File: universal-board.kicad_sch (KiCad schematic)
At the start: 15 parts, among them J1 USB_C_Receptacle, J2 CONN_I2C_GROVE, J3 CONN_WS2812, SW1 SW_RESET, U1 USBLC6-2SC6, U2 USBLC6-2SC6, U3 ESP32-S3-WROOM-1, U4 AMS1117-3.3

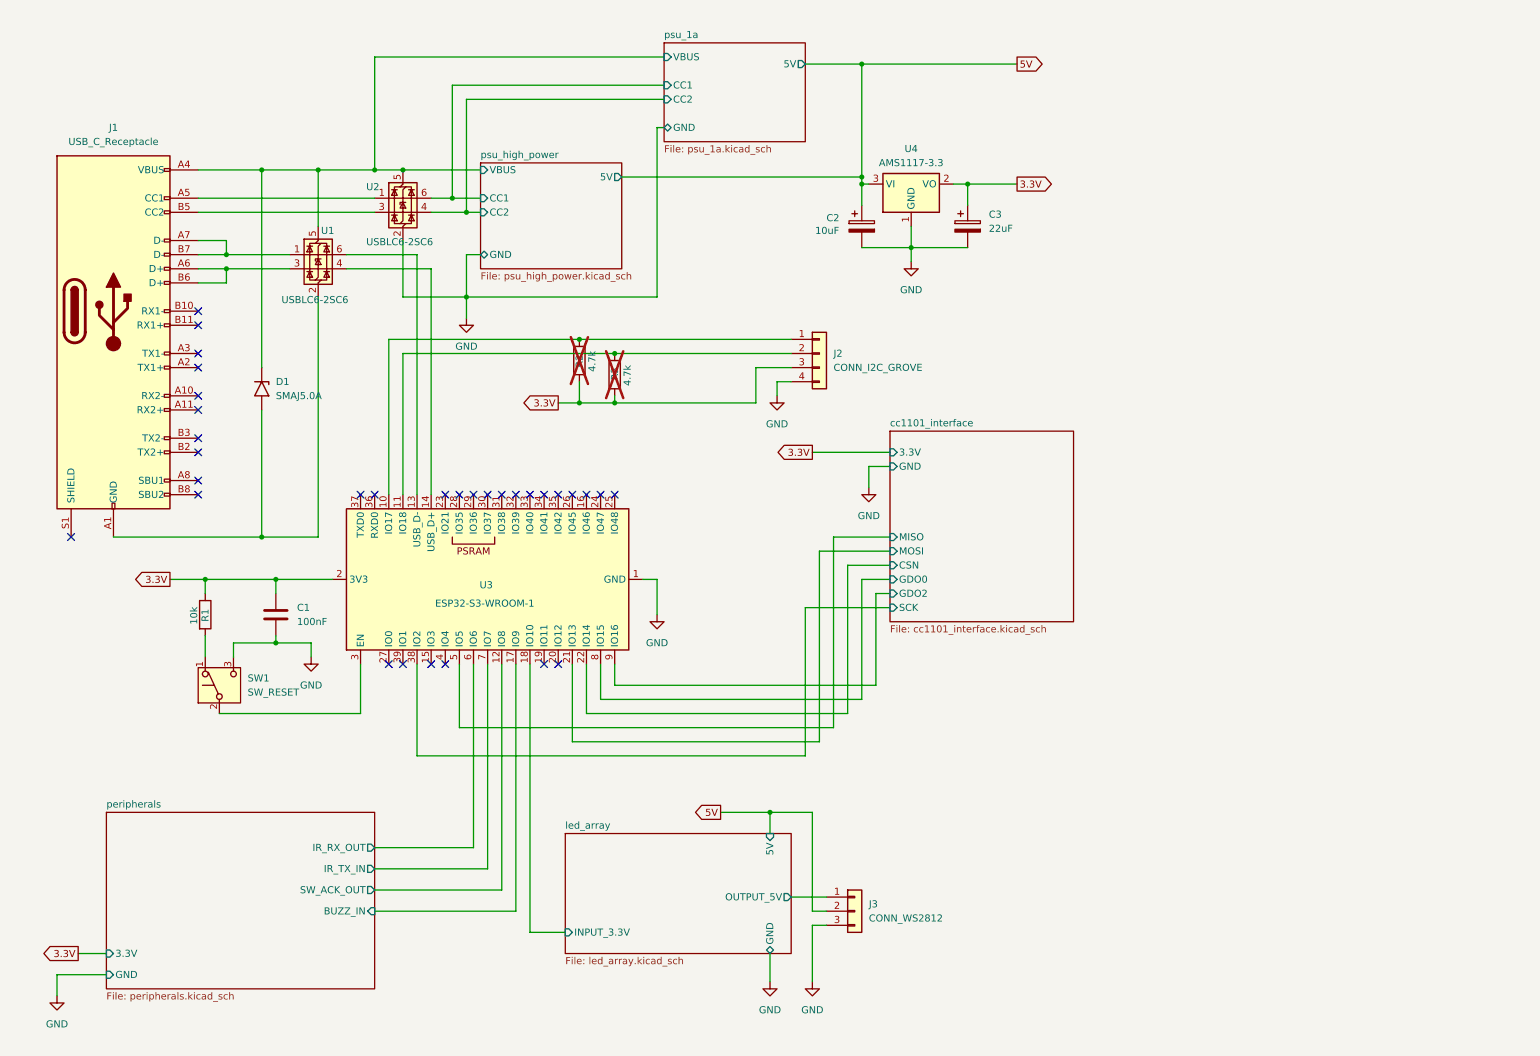
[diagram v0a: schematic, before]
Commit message: ERC fixes.
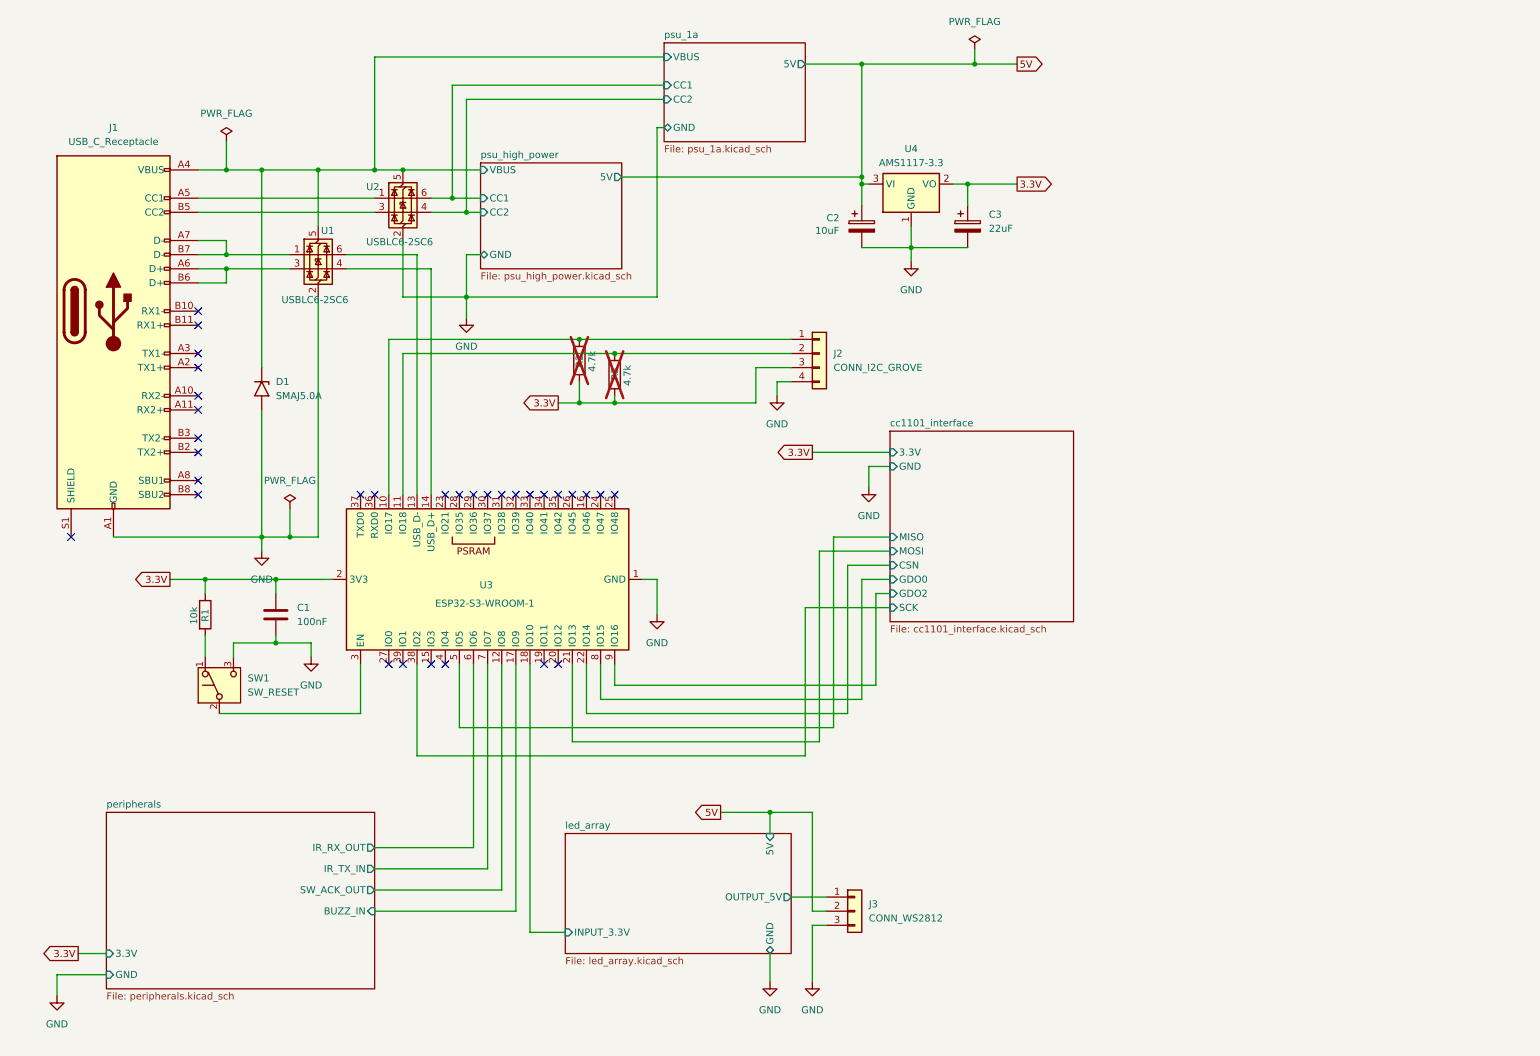
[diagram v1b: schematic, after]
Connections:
- net GND: now also D1.2 (A2), J1.A1 (GND), J1.A12 (GND), J1.B1 (GND), J1.B12 (GND), U1.2 (GND)

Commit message: - added bidirectional TVS between VBUS & GND - USB-C shield and GND are now connected - added comments re pin order - removed pull-up resistor on SW_ACK_INPUT because it's configured as INPUT_PULLUP
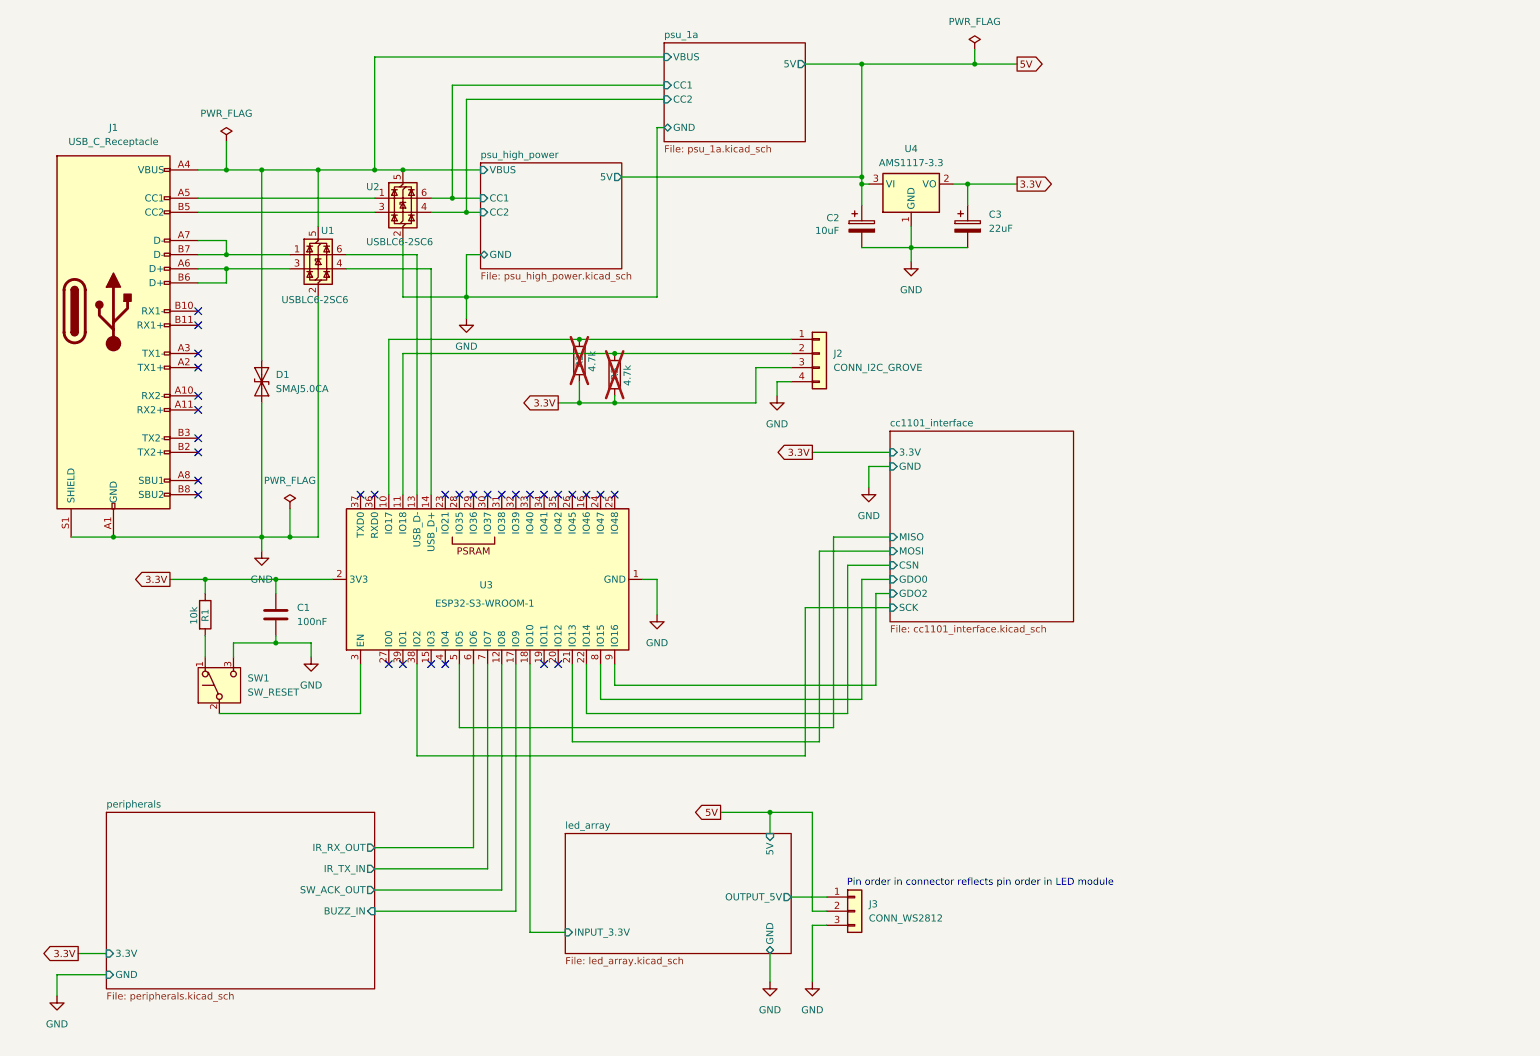
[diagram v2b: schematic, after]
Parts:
- removed D1: SMAJ5.0A, Diode_SMD:D_SMA, symbol Diode:SMAJ5.0A
- added D1: SMAJ5.0CA, Diode_SMD:D_SMA, symbol Diode:SMAJ5.0CA
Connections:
- net GND: now also J1.S1 (SHIELD), D1.1 (A1)
- net psu_1a/VBUS: now also D1.2 (A2)
- no-connect marks 32 -> 31
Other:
- note added: "Pin order in connector reflects pin order in LED module"
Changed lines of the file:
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@@
 	(generator_version "9.0")
 	(paper "A4")
+	(text "Pin order in connector reflects pin order in LED module"
+		(exclude_from_sim no)
+		(at 186.436 168.91 0)
+		(effects
+			(font
+				(size 1.27 1.27)
+			)
+		)
+	)
 	(junction
 		(at 148.59 156.21)
@@
 	)
 	(junction
+		(at 30.48 106.68)
+		(diameter 0)
+		(color 0 0 0 0)
+	)
+	(junction
 		(at 120.65 73.66)
 		(diameter 0)
@@
 	)
 	(no_connect
-		(at 22.86 106.68)
-	)
-	(no_connect
 		(at 102.87 99.06)
 	)
@@
 	(wire
 		(pts
-			(xy 67.31 40.64) (xy 57.15 40.64)
+			(xy 50.8 40.64) (xy 57.15 40.64)
 		)
 		(stroke
@@
 	(wire
 		(pts
-			(xy 57.15 40.64) (xy 50.8 40.64)
-		)
-		(stroke
-			(width 0)
-			(type default)
-		)
-	)
-	(wire
-		(pts
 			(xy 46.99 124.46) (xy 46.99 128.27)
 		)
@@
 	(wire
 		(pts
-			(xy 57.15 40.64) (xy 57.15 76.2)
-		)
-		(stroke
-			(width 0)
-			(type default)
-		)
-	)
-	(wire
-		(pts
 			(xy 165.1 135.89) (xy 165.1 114.3)
 		)
@@
 	(wire
 		(pts
-			(xy 57.15 83.82) (xy 57.15 106.68)
+			(xy 20.32 185.42) (xy 20.32 189.23)
 		)
 		(stroke
@@
 	(wire
 		(pts
-			(xy 20.32 185.42) (xy 20.32 189.23)
+			(xy 80.01 71.12) (xy 114.3 71.12)
 		)
 		(stroke
@@
 	(wire
 		(pts
-			(xy 80.01 71.12) (xy 114.3 71.12)
+			(xy 57.15 40.64) (xy 57.15 74.93)
 		)
 		(stroke
@@
 	(wire
 		(pts
+			(xy 22.86 106.68) (xy 30.48 106.68)
+		)
+		(stroke
+			(width 0)
+			(type default)
+		)
+	)
+	(wire
+		(pts
 			(xy 72.39 55.88) (xy 85.09 55.88)
 		)
@@
 	(wire
 		(pts
+			(xy 57.15 82.55) (xy 57.15 106.68)
+		)
+		(stroke
+			(width 0)
+			(type default)
+		)
+	)
+	(wire
+		(pts
 			(xy 77.47 40.64) (xy 82.55 40.64)
 		)
@@
 	(wire
 		(pts
+			(xy 57.15 40.64) (xy 67.31 40.64)
+		)
+		(stroke
+			(width 0)
+			(type default)
+		)
+	)
+	(wire
+		(pts
 			(xy 158.75 176.53) (xy 156.21 176.53)
 		)
@@
 		(dnp no)
 		(fields_autoplaced yes)
-		(property "Reference" "#PWR02"
+		(property "Reference" "#PWR03"
 			(at 66.04 134.62 0)
 			(effects
@@
 			(project ""
 				(path "/64404f27-cfd6-41d9-8edb-810ebab8cc14"
-					(reference "#PWR02")
+					(reference "#PWR03")
 					(unit 1)
 				)
@@
 	)
 	(symbol
-		(lib_id "Switch:SW_Push_SPDT")
-		(at 49.53 133.35 90)
+		(lib_id "Diode:SMAJ5.0CA")
+		(at 57.15 78.74 90)
 		(unit 1)
 		(exclude_from_sim no)
@@
 		(dnp no)
 		(fields_autoplaced yes)
-		(property "Reference" "SW1"
-			(at 54.61 132.0799 90)
+		(property "Reference" "D1"
+			(at 59.69 77.4699 90)
 			(effects
 				(font
@@
 			)
 		)
-		(property "Value" "SW_RESET"
-			(at 54.61 134.6199 90)
+		(property "Value" "SMAJ5.0CA"
+			(at 59.69 80.0099 90)
 			(effects
 				(font
@@
 			)
 		)
-		(property "Footprint" ""
-			(at 49.53 133.35 0)
+		(property "Footprint" "Diode_SMD:D_SMA"
+			(at 62.23 78.74 0)
 			(effects
 				(font
@@
 			)
 		)
-		(property "Datasheet" "~"
-			(at 49.53 133.35 0)
+		(property "Datasheet" "https://www.littelfuse.com/media?resourcetype=datasheets&itemid=75e32973-b177-4ee3-a0ff-cedaf1abdb93&filename=smaj-datasheet"
+			(at 57.15 78.74 0)
 			(effects
 				(font
@@
 			)
 		)
-		(property "Description" "Momentary Switch, single pole double throw"
-			(at 49.53 133.35 0)
+		(property "Description" "400W bidirectional Transient Voltage Suppressor, 5.0Vr, SMA(DO-214AC)"
+			(at 57.15 78.74 0)
 			(effects
 				(font
@@
 		(pin "2"
 		)
-		(pin "3"
-		)
 		(pin "1"
 		)
@@
 			(project ""
 				(path "/64404f27-cfd6-41d9-8edb-810ebab8cc14"
-					(reference "SW1")
+					(reference "D1")
 					(unit 1)
 				)
@@
 	)
 	(symbol
-		(lib_id "Diode:SMAJ5.0A")
-		(at 57.15 80.01 270)
+		(lib_id "Switch:SW_Push_SPDT")
+		(at 49.53 133.35 90)
 		(unit 1)
 		(exclude_from_sim no)
@@
 		(dnp no)
 		(fields_autoplaced yes)
-		(property "Reference" "D1"
-			(at 59.69 78.7399 90)
+		(property "Reference" "SW1"
+			(at 54.61 132.0799 90)
 			(effects
 				(font
 					(size 1.27 1.27)
 				)
-				(justify left)
+				(justify right)
 			)
 		)
-		(property "Value" "SMAJ5.0A"
-			(at 59.69 81.2799 90)
+		(property "Value" "SW_RESET"
+			(at 54.61 134.6199 90)
 			(effects
 				(font
 					(size 1.27 1.27)
 				)
-				(justify left)
+				(justify right)
 			)
 		)
-		(property "Footprint" "Diode_SMD:D_SMA"
-			(at 52.07 80.01 0)
+		(property "Footprint" ""
+			(at 49.53 133.35 0)
 			(effects
 				(font
@@
 			)
 		)
-		(property "Datasheet" "https://www.littelfuse.com/media?resourcetype=datasheets&itemid=75e32973-b177-4ee3-a0ff-cedaf1abdb93&filename=smaj-datasheet"
-			(at 57.15 78.74 0)
+		(property "Datasheet" "~"
+			(at 49.53 133.35 0)
 			(effects
 				(font
@@
 			)
 		)
-		(property "Description" "400W unidirectional Transient Voltage Suppressor, 5.0Vr, SMA(DO-214AC)"
-			(at 57.15 80.01 0)
+		(property "Description" "Momentary Switch, single pole double throw"
+			(at 49.53 133.35 0)
 			(effects
 				(font
@@
 		(pin "2"
 		)
+		(pin "3"
+		)
 		(pin "1"
 		)
 		(instances
-			(project "universal-board"
+			(project ""
 				(path "/64404f27-cfd6-41d9-8edb-810ebab8cc14"
-					(reference "D1")
+					(reference "SW1")
 					(unit 1)
 				)
@@
 		(dnp no)
 		(fields_autoplaced yes)
-		(property "Reference" "#PWR05"
+		(property "Reference" "#PWR06"
 			(at 148.59 193.04 0)
 			(effects
@@
 			(project ""
 				(path "/64404f27-cfd6-41d9-8edb-810ebab8cc14"
-					(reference "#PWR05")
+					(reference "#PWR06")
 					(unit 1)
 				)
@@
 		(dnp no)
 		(fields_autoplaced yes)
-		(property "Reference" "#FLG01"
+		(property "Reference" "#FLG03"
 			(at 185.42 17.145 0)
 			(effects
@@
 			(project ""
 				(path "/64404f27-cfd6-41d9-8edb-810ebab8cc14"
-					(reference "#FLG01")
+					(reference "#FLG03")
 					(unit 1)
 				)
@@
 		(dnp no)
 		(fields_autoplaced yes)
-		(property "Reference" "#PWR03"
+		(property "Reference" "#PWR04"
 			(at 93.98 73.66 0)
 			(effects
@@
 			(project ""
 				(path "/64404f27-cfd6-41d9-8edb-810ebab8cc14"
-					(reference "#PWR03")
+					(reference "#PWR04")
 					(unit 1)
 				)
@@
 		(dnp no)
 		(fields_autoplaced yes)
-		(property "Reference" "#FLG04"
+		(property "Reference" "#FLG01"
 			(at 50.8 33.655 0)
 			(effects
@@
 			(project ""
 				(path "/64404f27-cfd6-41d9-8edb-810ebab8cc14"
-					(reference "#FLG04")
+					(reference "#FLG01")
 					(unit 1)
 				)
@@
 		(dnp no)
 		(fields_autoplaced yes)
-		(property "Reference" "#PWR08"
+		(property "Reference" "#PWR09"
 			(at 166.37 104.14 0)
 			(effects
@@
 			(project ""
 				(path "/64404f27-cfd6-41d9-8edb-810ebab8cc14"
-					(reference "#PWR08")
+					(reference "#PWR09")
 					(unit 1)
 				)
@@
 		(dnp no)
 		(fields_autoplaced yes)
-		(property "Reference" "#PWR09"
+		(property "Reference" "#PWR010"
 			(at 173.99 63.5 0)
 			(effects
@@
 			(project ""
 				(path "/64404f27-cfd6-41d9-8edb-810ebab8cc14"
-					(reference "#PWR09")
+					(reference "#PWR010")
 					(unit 1)
 				)
@@
 		(dnp no)
 		(fields_autoplaced yes)
-		(property "Reference" "#FLG03"
+		(property "Reference" "#FLG02"
 			(at 62.23 99.695 0)
 			(effects
@@
 			(project ""
 				(path "/64404f27-cfd6-41d9-8edb-810ebab8cc14"
-					(reference "#FLG03")
+					(reference "#FLG02")
 					(unit 1)
 				)
@@
 		(dnp no)
 		(fields_autoplaced yes)
-		(property "Reference" "#PWR07"
+		(property "Reference" "#PWR08"
 			(at 156.21 193.04 0)
 			(effects
@@
 			(project ""
 				(path "/64404f27-cfd6-41d9-8edb-810ebab8cc14"
-					(reference "#PWR07")
+					(reference "#PWR08")
 					(unit 1)
 				)
@@
 		(dnp no)
 		(fields_autoplaced yes)
-		(property "Reference" "#PWR04"
+		(property "Reference" "#PWR05"
 			(at 128.27 127 0)
 			(effects
@@
 			(project ""
 				(path "/64404f27-cfd6-41d9-8edb-810ebab8cc14"
-					(reference "#PWR04")
+					(reference "#PWR05")
 					(unit 1)
 				)
@@
 		(dnp no)
 		(fields_autoplaced yes)
-		(property "Reference" "#PWR010"
+		(property "Reference" "#PWR02"
 			(at 57.15 115.57 0)
 			(effects
@@
 			(project ""
 				(path "/64404f27-cfd6-41d9-8edb-810ebab8cc14"
-					(reference "#PWR010")
+					(reference "#PWR02")
 					(unit 1)
 				)
@@
 		(dnp no)
 		(fields_autoplaced yes)
-		(property "Reference" "#PWR06"
+		(property "Reference" "#PWR07"
 			(at 149.86 87.63 0)
 			(effects
@@
 			(project ""
 				(path "/64404f27-cfd6-41d9-8edb-810ebab8cc14"
-					(reference "#PWR06")
+					(reference "#PWR07")
 					(unit 1)
 				)

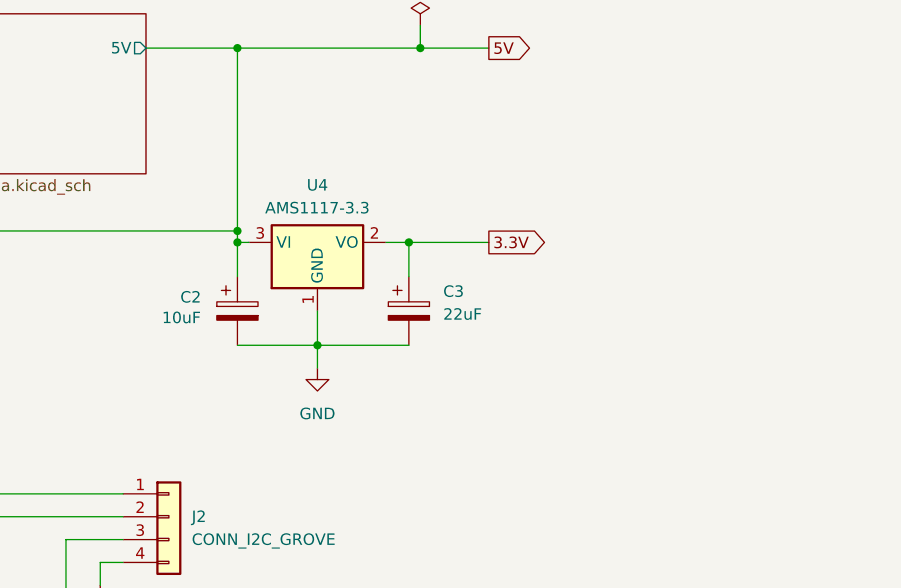
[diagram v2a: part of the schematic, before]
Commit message: Added decoupling caps for the AMS1117-3.3
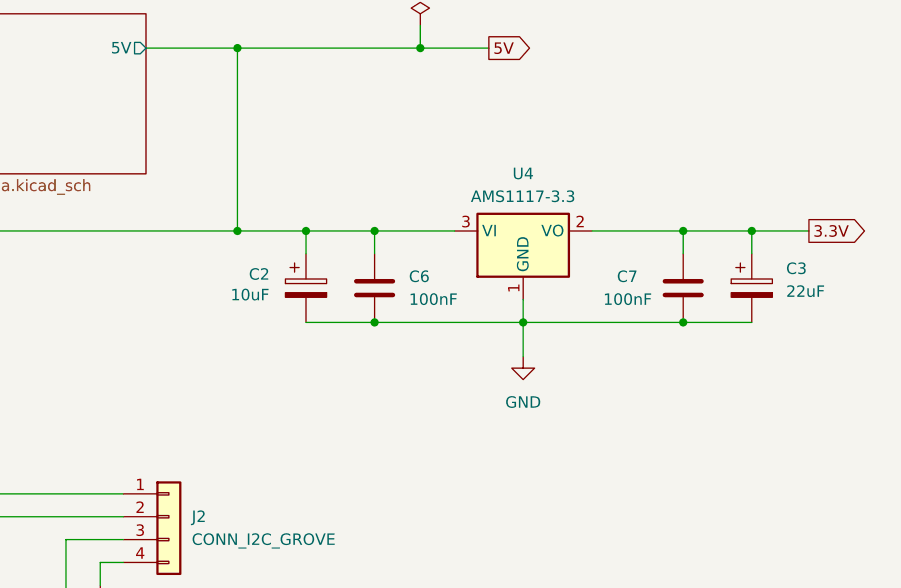
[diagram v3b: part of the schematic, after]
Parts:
- added C6, C7: 100nF, symbol Device:C
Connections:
- net 3.3V: now also C7.1
- net 5V: now also C6.1
- net GND: now also C6.2, C7.2
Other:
- moved on the sheet: C2, C3, U4
